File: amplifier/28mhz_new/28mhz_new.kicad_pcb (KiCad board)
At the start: 2 copper layers, 89 x 41 mm, 33 parts, among them M1 RD16HHF1

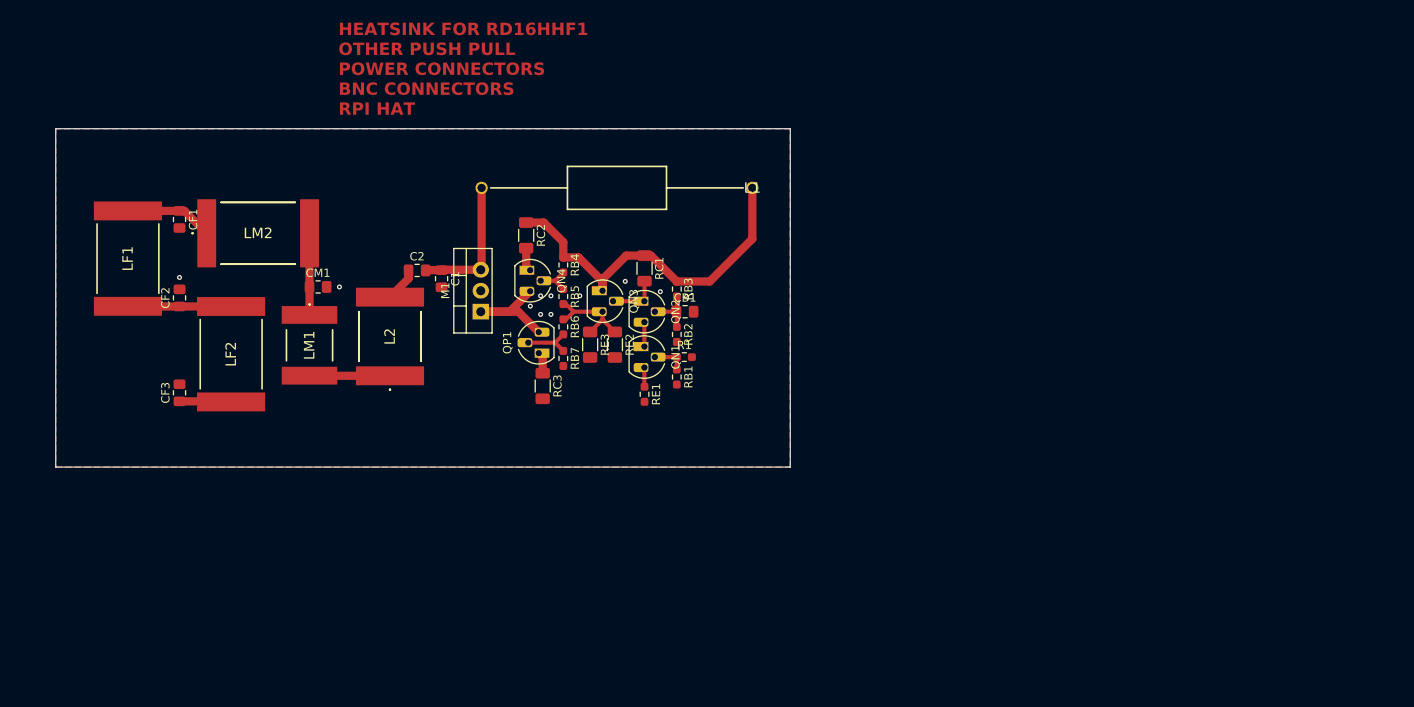
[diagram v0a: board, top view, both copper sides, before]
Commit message: This looks nice, but I'm realizing soldering it will be basically impossible
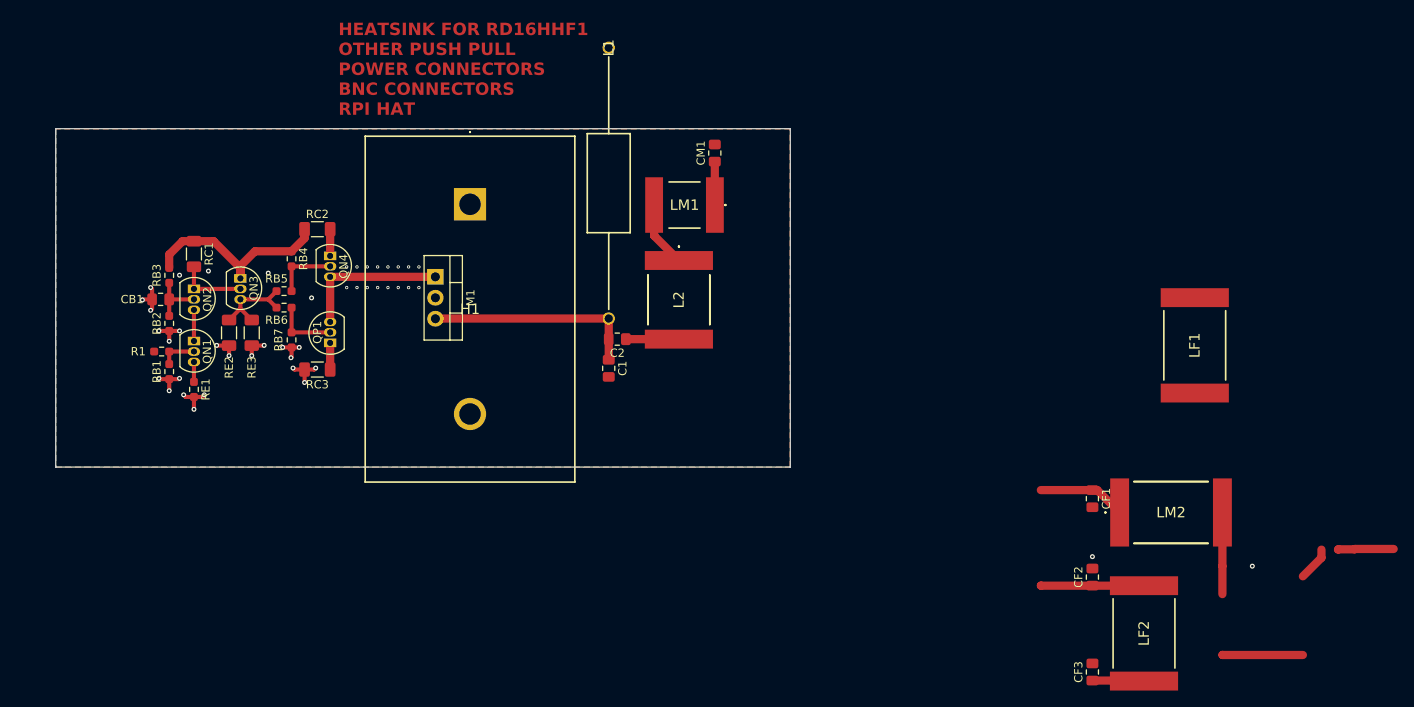
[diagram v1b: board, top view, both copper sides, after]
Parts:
- added H1: 647-25ABPE, heatsink:64725ABPE, F.Cu at (117.2, 79.2)
- QN1, QN2, QN3, QN4, QP1: footprint Package_TO_SOT_THT:TO-92L_HandSolder -> Package_TO_SOT_THT:TO-92L_Inline
- moved LF1 129.7 mm to (205.0, 96.2)
- moved CF1 115.7 mm to (192.6, 114.8)
- moved CF2 115.7 mm to (192.6, 124.3)
- moved CF3 115.7 mm to (192.6, 135.8)
- moved LF2 115.7 mm to (198.8, 131.1)
- moved LM2 115.7 mm to (202.1, 116.5)
- moved CB1 63.6 mm to (79.7, 90.7), turned to 180 degrees
- moved R1 63.3 mm to (79.8, 97.0), turned to 180 degrees
- moved RB3 61.5 mm to (80.8, 87.8)
- moved RB2 61.5 mm to (80.8, 93.6)
- moved RB1 61.5 mm to (80.8, 99.4)
- moved RC1 54.6 mm to (83.8, 85.2)
- moved RE1 54.6 mm to (83.8, 101.6)
- moved QN2 54.6 mm to (83.8, 89.4)
- moved QN1 54.6 mm to (83.8, 95.7)
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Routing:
- net 0: track 0.00 -> 29.3 mm, vias 10 -> 44
- net /VCC: track 44.8 -> 25.3 mm
- net Net-(M1-D): track 16.9 -> 32.9 mm
- net Net-(L2-Pad1): track 9.76 -> 17.9 mm
- net Net-(C2-Pad1): track 4.17 -> 10.6 mm
- net Net-(CM1-Pad1): track 9.89 -> 15.2 mm
- net Net-(M1-G): track 15.0 -> 18.2 mm
- net Net-(QN4-B): track 4.58 -> 7.67 mm
- net Net-(QN2-C): track 6.26 -> 8.30 mm
- net Net-(QP1-B): track 6.08 -> 7.67 mm
- net Net-(QN1-C): track 2.96 -> 3.78 mm
- net Net-(QN3-E): track 12.0 -> 11.2 mm
- net Net-(QN2-B): track 6.33 -> 7.00 mm
- net Net-(QP1-C): track 2.63 -> 3.23 mm

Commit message: NO DRC ERRORS
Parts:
- added J1: Conn_Coaxial_Small, BNC:CONBNC002, F.Cu at (76.3, 103.0)
- added J1: GPIO, Connector_PinSocket_2.54mm:PinSocket_2x20_P2.54mm_Vertical, B.Cu at (80.4, 66.7)
- R1: footprint Resistor_SMD:R_0603_1608Metric_Pad0.98x0.95mm_HandSolder -> Resistor_SMD:R_1206_3216Metric_Pad1.30x1.75mm_HandSolder
- RB1, RB2, RB3, RB4, RB5, RB6, RB7, RE1: footprint Resistor_SMD:R_0603_1608Metric_Pad0.98x0.95mm_HandSolder -> Resistor_SMD:R_0805_2012Metric_Pad1.20x1.40mm_HandSolder
- moved LF2 134.4 mm to (70.5, 91.2)
- moved CF3 123.1 mm to (74.8, 100.2), turned to 0 degrees
- moved LF1 120.0 mm to (85.0, 94.5), turned to 0 degrees
- moved CF2 119.8 mm to (78.5, 87.8), turned to 0 degrees
- moved LM2 112.9 mm to (89.5, 108.2), turned to -90 degrees
- moved CF1 98.9 mm to (95.0, 98.8), turned to 0 degrees
- moved CM1 63.5 mm to (96.0, 111.0)
- moved LM1 51.8 mm to (103.0, 112.0), turned to 0 degrees
- moved L2 40.2 mm to (103.5, 100.5), turned to 90 degrees
- moved L1 33.9 mm to (101.6, 70.2), turned to 0 degrees
- moved C2 23.3 mm to (111.8, 97.0), turned to 0 degrees
- moved C1 19.0 mm to (115.0, 98.0)
- moved RE1 14.7 mm to (89.0, 87.9), turned to 0 degrees
- moved RB5 14.0 mm to (98.8, 76.3)
- moved RB3 13.8 mm to (85.0, 74.7)
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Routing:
- net 0: track 29.3 -> 0.00 mm, vias 44 -> 36
- net /RF_IN: track 0.00 -> 21.0 mm
- net Net-(L2-Pad1): track 17.9 -> 8.04 mm
- net Net-(M1-G): track 18.2 -> 26.9 mm
- net Net-(M1-D): track 32.9 -> 38.9 mm
- net Net-(CM1-Pad1): track 15.2 -> 10.8 mm
- net /VCC: track 25.3 -> 29.3 mm
- net Net-(QN3-E): track 11.2 -> 14.5 mm
- net Net-(C2-Pad1): track 10.6 -> 7.73 mm
- net Net-(QN4-B): track 7.67 -> 5.24 mm
- net Net-(CF2-Pad1): track 12.5 -> 14.4 mm
- net Net-(QN4-C): track 3.23 -> 4.91 mm
- net Net-(CF1-Pad1): track 10.7 -> 11.9 mm
- net Net-(QP1-B): track 7.67 -> 6.58 mm
- net /RF_OUT: track 6.28 -> 7.35 mm
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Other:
- board size 89 x 41 mm -> 73.2 x 56 mm
- board text added: "DISPLAY (OPTIONAL)"
- board text added: "Extend PCB edge 0.5mm if using SMT header"
- board text added: "PoE"
- board text added: "RJ45"
- board text added: "USB"
